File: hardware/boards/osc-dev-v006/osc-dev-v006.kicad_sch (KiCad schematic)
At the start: 4 parts

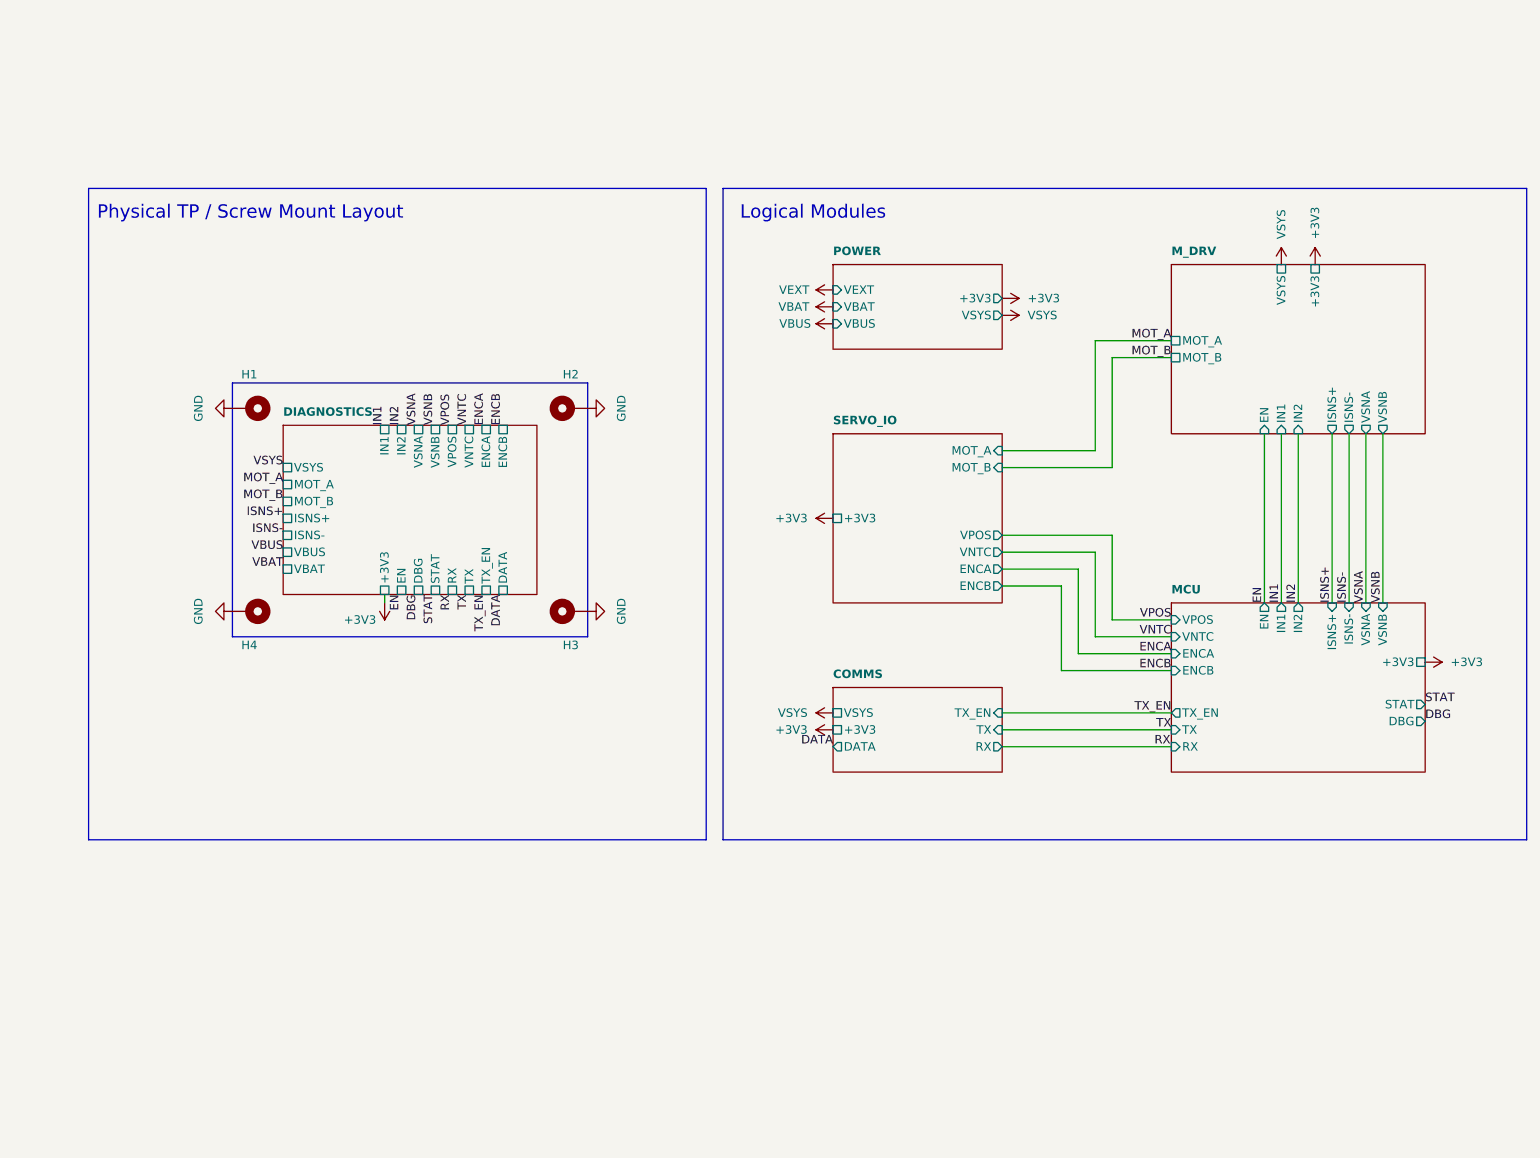
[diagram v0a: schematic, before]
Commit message: OSC DEV CH32 REV B (#10)
* update board

* updated schematics. ERC on schematics is now passing

* completed routing.

* adding ground vias

* update schematics notes

* update bom and component properties

* use red header pins for jumpers

* rename board to osc-dev-v006

* add docs
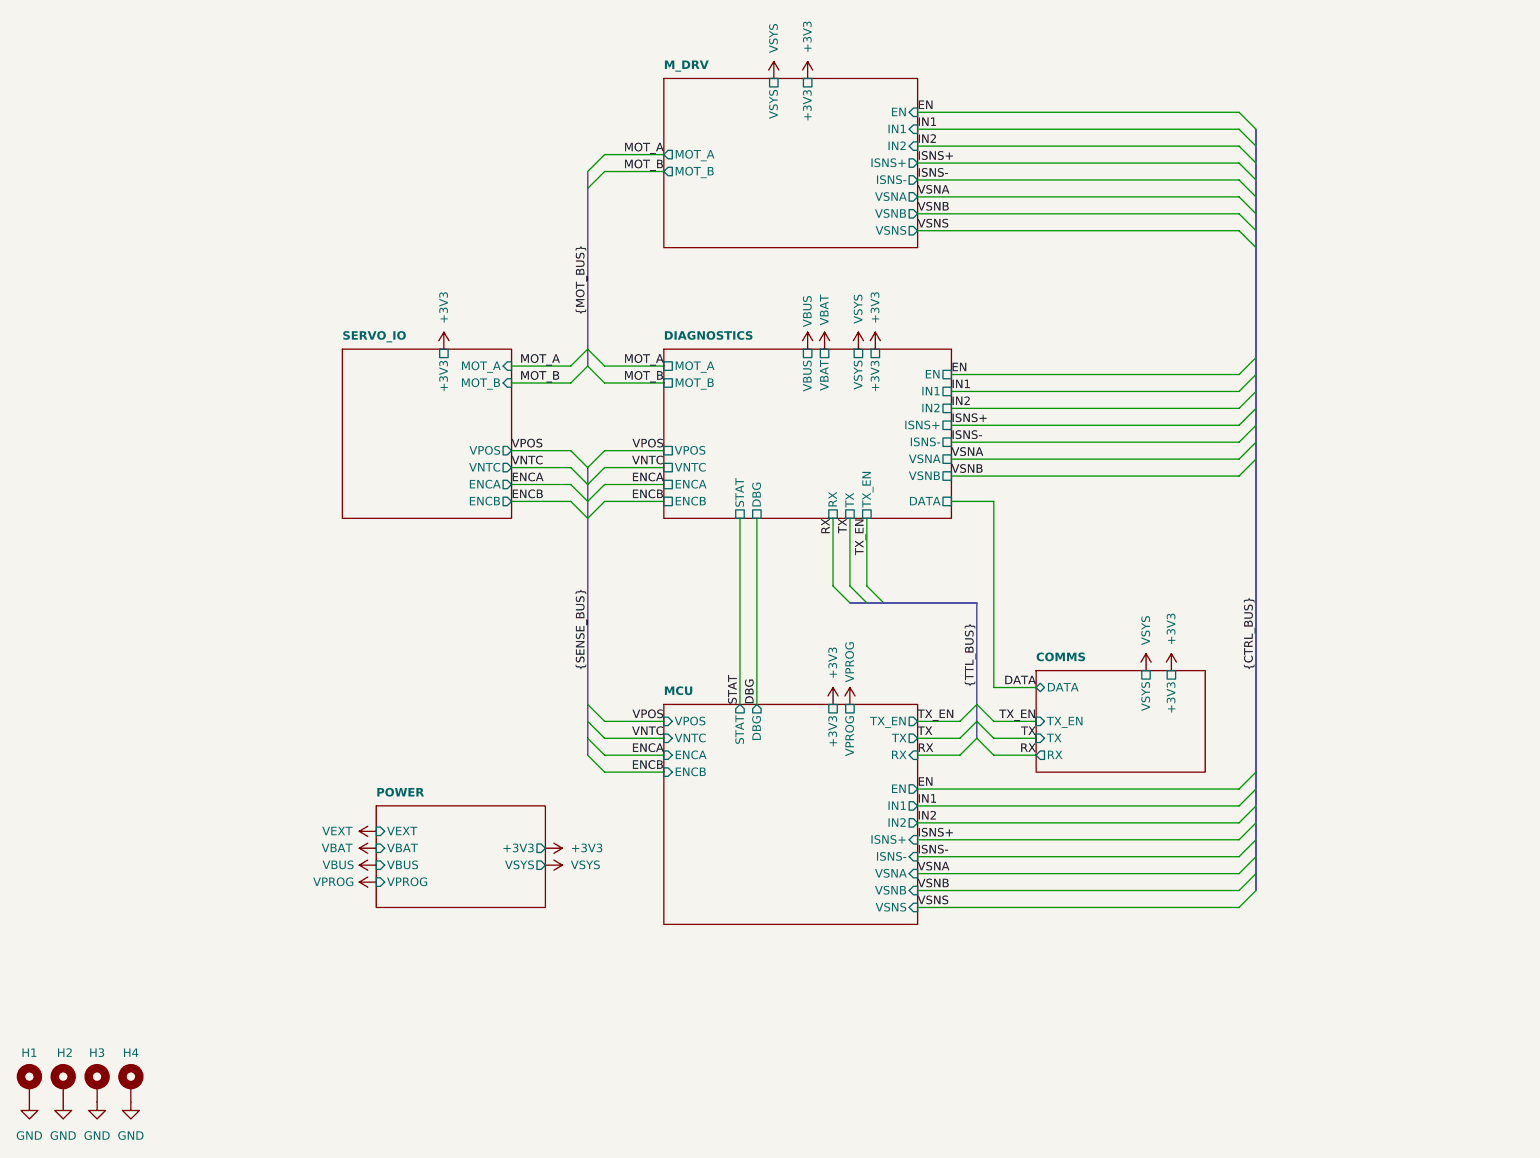
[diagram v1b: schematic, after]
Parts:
- renumbered H4 to H2, H2 to H3, H3 to H4
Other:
- sheet MCU ports: added VPROG, VSNS; removed none
- sheet M_DRV ports: added VSNS; removed none
- sheet POWER ports: added VPROG; removed none
- note removed: "Logical Modules"
- note removed: "Physical TP / Screw Mount Layout"
- moved on the sheet: H1, H2, H3, H4
